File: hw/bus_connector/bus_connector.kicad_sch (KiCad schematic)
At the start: 9 parts, among them J1 DE9_Left, J2 DE9_Top, J3 DE9_Right

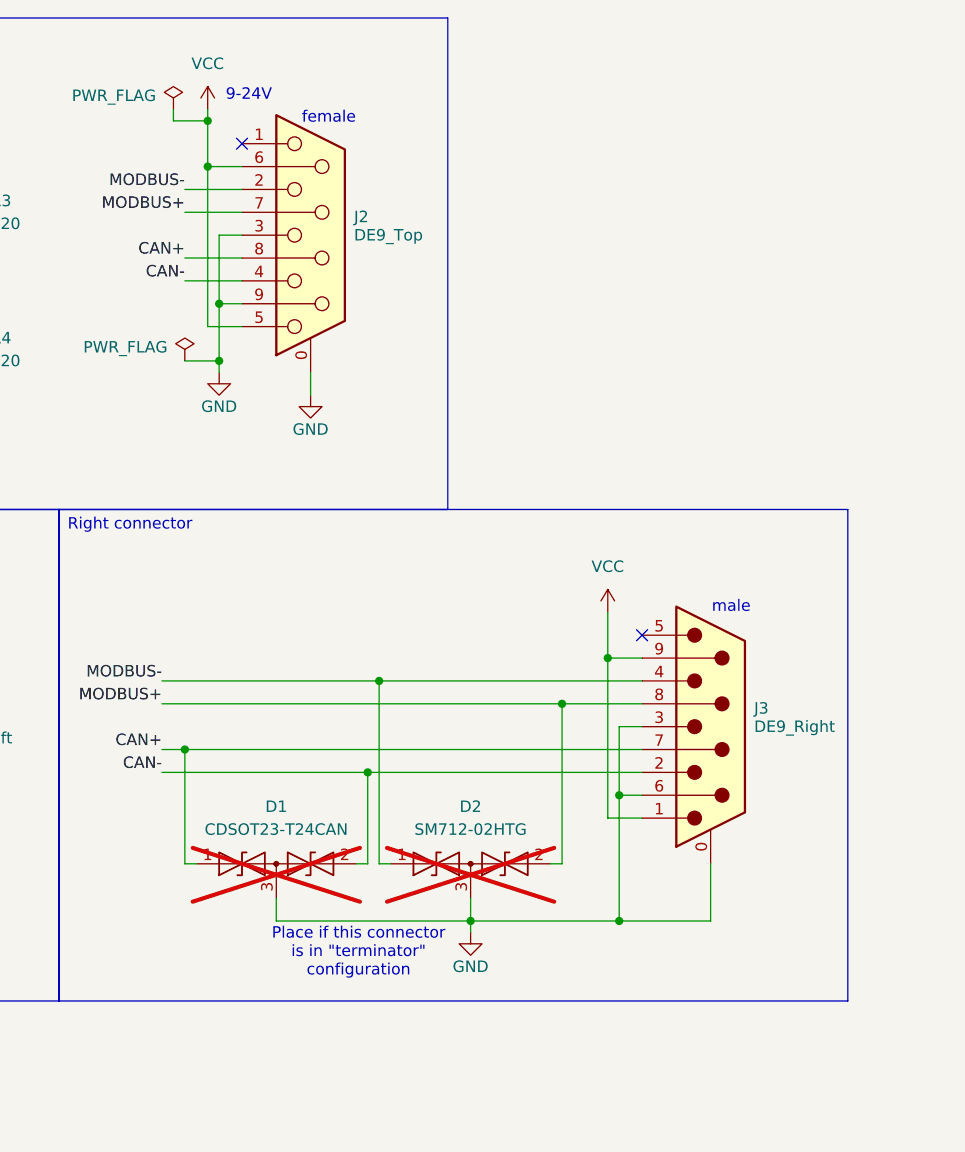
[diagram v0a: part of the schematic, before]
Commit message: Add test points
Signed-off-by: Mateusz Pająk <22417805+Tai-Min@users.noreply.github.com>
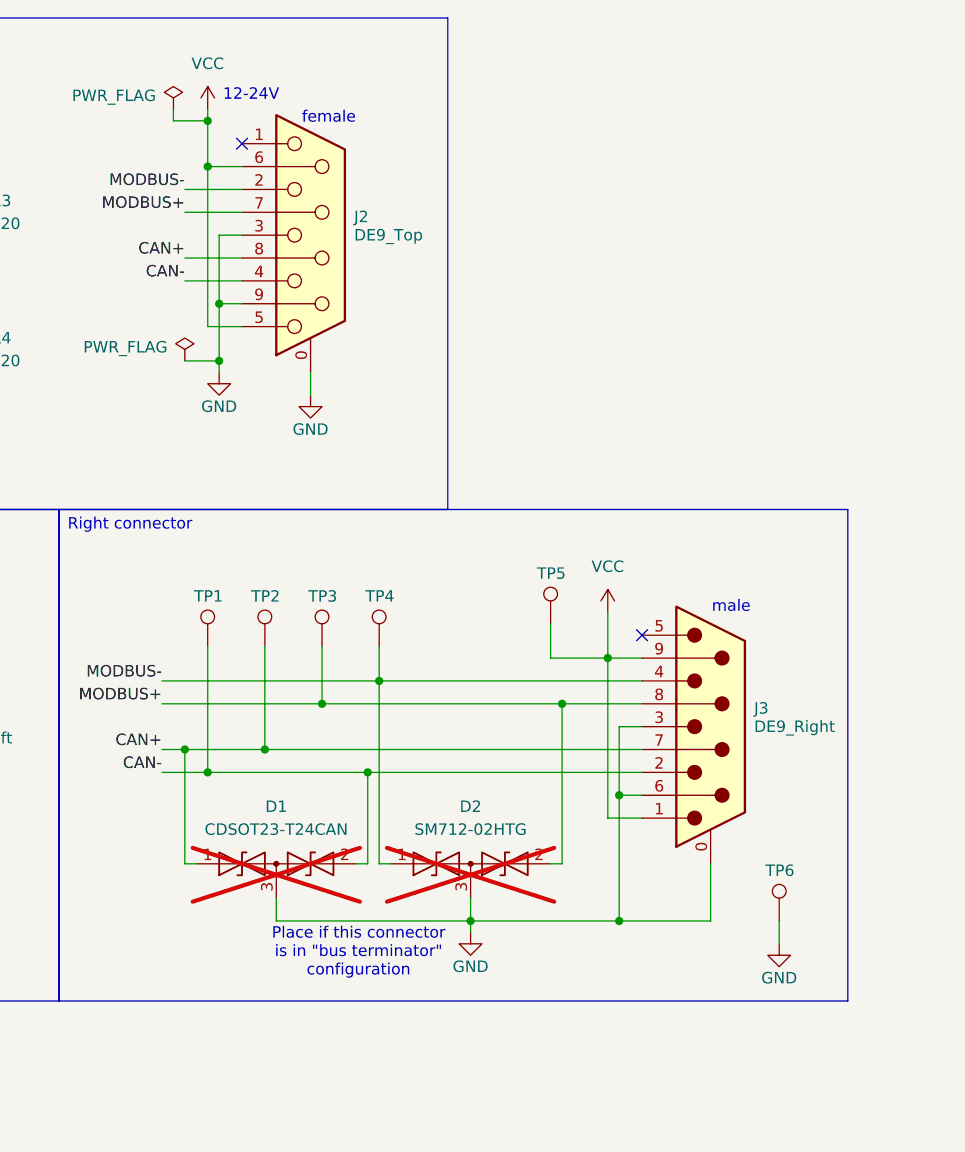
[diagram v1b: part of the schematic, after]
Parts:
- added TP1, TP2, TP3, TP4, TP5, TP6: TestPoint, TestPoint:TestPoint_Pad_D1.5mm, symbol Connector:TestPoint
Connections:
- net CAN+: now also TP2.1
- net CAN-: now also TP1.1
- net GND: now also TP6.1
- net MODBUS+: now also TP3.1
- net MODBUS-: now also TP4.1
- net VCC: now also TP5.1
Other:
- note added: "12-24V"
- note removed: "9-24V"
- note removed: "Place if this connector is in "terminator" configuration"

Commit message: Change versioning
Signed-off-by: Mateusz Pająk <22417805+Tai-Min@users.noreply.github.com>
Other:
- note added: "Place if this connector is in "bus terminator" or "bus connector" configuration"
- title: Bus Connector -> ${TITLE}
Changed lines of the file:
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@@
 	(paper "A4")
 	(title_block
-		(title "Bus Connector")
+		(title "${TITLE}")
 		(date "2025-11-24")
-		(rev "1.0")
+		(rev "${REVISION}")
 	)
 	(rectangle
@@
 		)
 	)
-	(text "Place if this connector\nis in \"bus terminator\" \nconfiguration"
+	(text "Place if this connector\nis in \"bus terminator\" or \n\"bus connector\" configuration"
 		(exclude_from_sim no)
-		(at 185.674 140.716 0)
+		(at 181.356 140.716 0)
 		(effects
 			(font

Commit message: Redo vias and VCC
Signed-off-by: Mateusz Pająk <22417805+Tai-Min@users.noreply.github.com>
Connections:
- net CAN+: now also D1.2 (A2); no longer D1.1 (A1)
- net CAN-: now also D1.1 (A1); no longer D1.2 (A2)
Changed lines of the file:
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@@
 		(lib_id "Diode:SM712_SOT23")
 		(at 176.53 130.81 0)
+		(mirror y)
 		(unit 1)
 		(exclude_from_sim no)
@@
 		(on_board yes)
 		(dnp yes)
-		(fields_autoplaced yes)
 		(property "Reference" "D1"
 			(at 176.53 124.46 0)
@@
 		)
 		(property "Datasheet" "\\datasheets\\CDSOT23-T24CAN.pdf"
-			(at 172.72 130.81 0)
+			(at 180.34 130.81 0)
 			(effects
 				(font

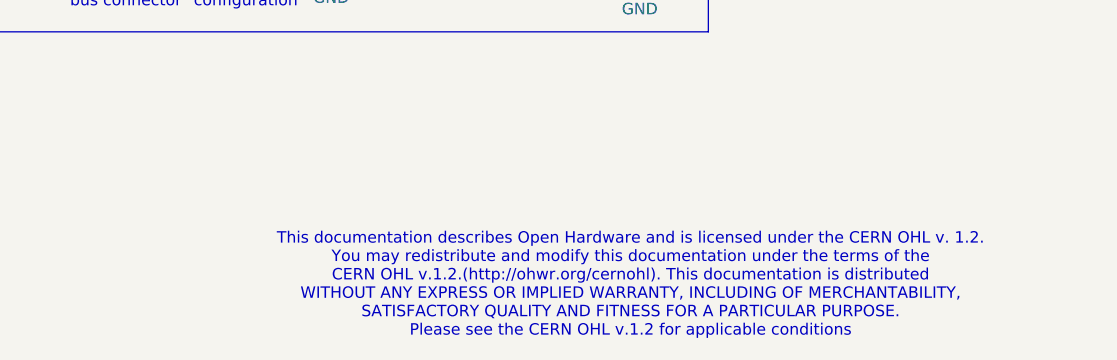
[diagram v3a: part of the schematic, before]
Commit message: Add proper drawing sheet with license
Signed-off-by: Mateusz Pająk <22417805+Tai-Min@users.noreply.github.com>
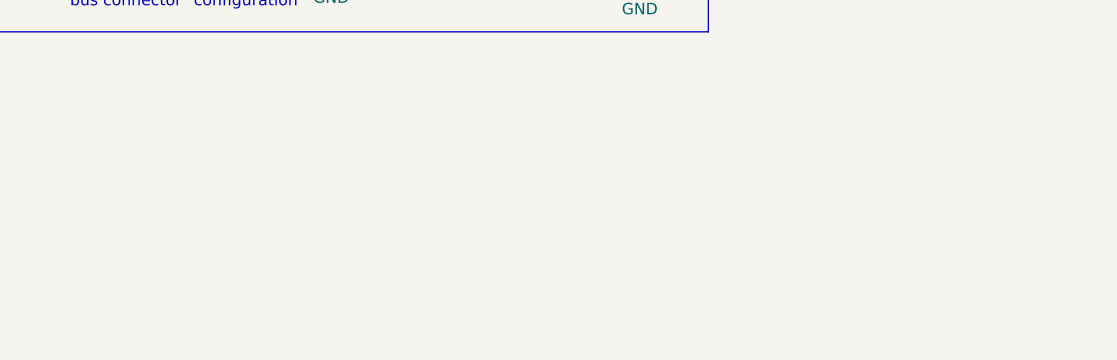
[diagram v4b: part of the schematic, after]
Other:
- note removed: "This documentation describes Open Hardware and is licensed under the CERN OHL v. 1.2. You may redistribute and modify this documentation under the terms of the CERN OHL v.1.2.(http://ohwr.org/cernohl). This documentation is distributed WITHOUT ANY EXPRESS OR IMPLIED WARRANTY, INCLUDING OF MERCHANTABILITY, SATISFACTORY QUALITY AND FITNESS FOR A PARTICULAR PURPOSE. Please see the CERN OHL v.1.2 for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"
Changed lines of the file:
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@@
-		)
-	)
-	(text "This documentation describes Open Hardware and is licensed under the CERN OHL v. 1.2.\nYou may redistribute and modify this documentation under the terms of the \nCERN OHL v.1.2.(http://ohwr.org/cernohl). This documentation is distributed \nWITHOUT ANY EXPRESS OR IMPLIED WARRANTY, INCLUDING OF MERCHANTABILITY,\nSATISFACTORY QUALITY AND FITNESS FOR A PARTICULAR PURPOSE.\nPlease see the CERN OHL v.1.2 for applicable conditions"
-		(exclude_from_sim no)
-		(at 231.394 174.244 0)
-		(effects
-			(font
-				(size 1.27 1.27)
-			)
 		)
 	)
@@
 	)
 	(embedded_fonts no)
+	(embedded_files
+		(file
+			(name "drawing_sheet.kicad_wks")
+			(type worksheet)
+			(data |KLUv/WAhCq0bANZtjiDgWjeUd7GfIpdQ3hsyJE4imh40WCrg3bHZNmcww0sw4IEAhQCDAL5lJzOj
+				pT+67/YvbT+xKmvrmW/8KFQ2Oef8xK9I+Farb213mmX+KIu3+RqV985lKu8S6eqtOr4kbVGiPXrU
+				0FVt89I+L+vxRQ2dVv1fN92t3wUAICBIqfanm+bIRNk9X4SmMtd5W/34SYZGrTXBbZzjfFP9qwIg
+				IEhPLNFpzXsqBJlvi9J55PpTNhS/0Av/dccTzaUrOLDziasXG43MLVVTuGOrGQ04il9HJPEioAVG
+				6LTOt1od2sIZjdhHehLRxxlHEEbwx28r0Vq79G/8prtGd6cqU8d59Vxc51tZlltNFAAb51H1jvM0
+				p7Ka+W79Lne3JTrOt87V0ia+237qtX6ss7lR3wKlAg6Nsqco/XufGbVV5dU7vedrd1mUqzIIhzRO
+				q66t/FLReEb8Iv6l7fpPrPLzU/zmRT29fmLrry3r1Lbi+FMaT7+82kz/dJzvtiozn57eErfgOgej
+				Qnoh+X2VsdFIaAqMl/ku4OROzIvafZ2hbfW7kCCJ7ktylavn9f1fGgeI2OAEAwGBgds6bcG5o+HQ
+				GOk9cTb90dKaF02lrP+n/ql9NMQh7Rs1ocgJXfQunAhIil7o3iRDghOXeJyNg0QNGfEmI0h6Iw6B
+				FxDiVSLih/GJxikZUMK5RDKgH0BkxhNFz+OSD7yEGNBFjY/jJ4afz0EZz0mOpkKCntM1A1rKWL+J
+				IOmsaVYpIxCP1N4BgIagATmGmBkakSCSpCDJcGBExMxVN+ZEMIr2+Ixg+w44oI2QkWfDYQBGWKkF
+				Mwg4uwAUEVRASQ6CoSO7wOH2oRcJQ92PVxKzOyKxApiF5j1bCYde/8e8NSfJCOTZBjnL5kEgk9zl
+				MlBII26C1dPzpy84m5fIib7lme/qD5PyoQz2EJoQE1jDRgTxITi8ia/sl5+zrDxPhKBBn57ycYJg
+				ZCwqHFwyZdBoqHYp0zBZO06dzgfsT4kYixZyxQyfvGf1jGnpkx8aKmozkcOWchtBzaWzZv2hQIju
+				lOqJaiUvzvCA3LzBdbUVIJOYJSx0+3ufDFvX5dIvDoxARYL0gCYirRADAnCnk8CcCCxLwcP0pwGD
+				AcdTPbjcedGBdAsSMjEiw0/8xNymVps2TR/W8jcsl1Bj2egAHQNMBQ==|
+			)
+			(checksum "F4CA3C5331BFF1A6D590C818164A77B8")
+		)
+	)
 )

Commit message: Update LCSC BOM
Signed-off-by: Mateusz Pająk <22417805+Tai-Min@users.noreply.github.com>
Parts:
- D1: LCSC https://www.lcsc.com/product-detail/C2959841.html?s_z=n_CDS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 -> (none); LCSC Link (none) -> https://www.lcsc.com/product-detail/C2959841.html?s_z=n_CDS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; LCSC Part # (none) -> C2959841
- D2: LCSC https://www.lcsc.com/product-detail/C172881.html?s_z=n_SM712 -> (none); LCSC Link (none) -> https://www.lcsc.com/product-detail/C172881.html?s_z=n_SM712; LCSC Part # (none) -> C172881
- J1, J2: LCSC https://www.lcsc.com/product-detail/C19077337.html?s_z=n_XU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 -> (none); LCSC Link (none) -> https://www.lcsc.com/product-detail/C19077337.html?s_z=n_XU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; LCSC Part # (none) -> C19077337
- J3: LCSC https://www.lcsc.com/product-detail/C19077344.html?s_z=n_ds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 -> (none); LCSC Link (none) -> https://www.lcsc.com/product-detail/C19077344.html?s_z=n_ds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; LCSC Part # (none) -> C19077344
- R1, R2, R3, R4: LCSC https://www.lcsc.com/product-detail/C114928.html -> (none); LCSC Link (none) -> https://www.lcsc.com/product-detail/C114928.html; LCSC Part # (none) -> C114928
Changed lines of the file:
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@@
 			)
 		)
-		(property "LCSC" "https://www.lcsc.com/product-detail/C114928.html"
+		(property "LCSC Link" "https://www.lcsc.com/product-detail/C114928.html"
+			(at 96.52 119.38 0)
+			(effects
+				(font
+					(size 1.27 1.27)
+				)
+				(hide yes)
+			)
+		)
+		(property "LCSC Part #" "C114928"
 			(at 96.52 119.38 0)
 			(effects
@@
 			)
 		)
+		(property "LCSC Part #" ""
+			(at 168.91 106.68 0)
+			(effects
+				(font
+					(size 1.27 1.27)
+				)
+				(hide yes)
+			)
+		)
 		(pin "1"
 		)
@@
 			)
 		)
-		(property "LCSC" "https://www.lcsc.com/product-detail/C19077344.html?s_z=n_dsub"
+		(property "LCSC Link" "https://www.lcsc.com/product-detail/C19077344.html?s_z=n_dsub"
+			(at 224.79 115.57 0)
+			(effects
+				(font
+					(size 1.27 1.27)
+				)
+				(hide yes)
+			)
+		)
+		(property "LCSC Part #" "C19077344"
 			(at 224.79 115.57 0)
 			(effects
@@
 		)
 		(property "Description" "test point"
+			(at 232.41 137.16 0)
+			(effects
+				(font
+					(size 1.27 1.27)
+				)
+				(hide yes)
+			)
+		)
+		(property "LCSC Part #" ""
 			(at 232.41 137.16 0)
 			(effects
@@
 			)
 		)
-		(property "LCSC" "https://www.lcsc.com/product-detail/C114928.html"
+		(property "LCSC Link" "https://www.lcsc.com/product-detail/C114928.html"
+			(at 142.24 58.42 0)
+			(effects
+				(font
+					(size 1.27 1.27)
+				)
+				(hide yes)
+			)
+		)
+		(property "LCSC Part #" "C114928"
 			(at 142.24 58.42 0)
 			(effects
@@
 		)
 		(property "Description" "test point"
+			(at 187.96 106.68 0)
+			(effects
+				(font
+					(size 1.27 1.27)
+				)
+				(hide yes)
+			)
+		)
+		(property "LCSC Part #" ""
 			(at 187.96 106.68 0)
 			(effects
@@
 			)
 		)
-		(property "LCSC" "https://www.lcsc.com/product-detail/C114928.html"
+		(property "LCSC Link" "https://www.lcsc.com/product-detail/C114928.html"
+			(at 142.24 73.66 0)
+			(effects
+				(font
+					(size 1.27 1.27)
+				)
+				(hide yes)
+			)
+		)
+		(property "LCSC Part #" "C114928"
 			(at 142.24 73.66 0)
 			(effects
@@
 			)
 		)
+		(property "LCSC Part #" ""
+			(at 181.61 106.68 0)
+			(effects
+				(font
+					(size 1.27 1.27)
+				)
+				(hide yes)
+			)
+		)
 		(pin "1"
 		)
@@
 			)
 		)
-		(property "LCSC" "https://www.lcsc.com/product-detail/C114928.html"
+		(property "LCSC Link" "https://www.lcsc.com/product-detail/C114928.html"
+			(at 96.52 104.14 0)
+			(effects
+				(font
+					(size 1.27 1.27)
+				)
+				(hide yes)
+			)
+		)
+		(property "LCSC Part #" "C114928"
 			(at 96.52 104.14 0)
 			(effects
@@
 		)
 		(property "Description" "test point"
+			(at 175.26 106.68 0)
+			(effects
+				(font
+					(size 1.27 1.27)
+				)
+				(hide yes)
+			)
+		)
+		(property "LCSC Part #" ""
 			(at 175.26 106.68 0)
 			(effects
@@
 			)
 		)
-		(property "LCSC" "https://www.lcsc.com/product-detail/C172881.html?s_z=n_SM712"
+		(property "LCSC Link" "https://www.lcsc.com/product-detail/C172881.html?s_z=n_SM712"
+			(at 198.12 130.81 0)
+			(effects
+				(font
+					(size 1.27 1.27)
+				)
+				(hide yes)
+			)
+		)
+		(property "LCSC Part #" "C172881"
 			(at 198.12 130.81 0)
 			(effects
@@
 			)
 		)
-		(property "LCSC" "https://www.lcsc.com/product-detail/C2959841.html?s_z=n_CDSOT23-T24CAN"
+		(property "LCSC Link" "https://www.lcsc.com/product-detail/C2959841.html?s_z=n_CDSOT23-T24CAN"
+			(at 176.53 130.81 0)
+			(effects
+				(font
+					(size 1.27 1.27)
+				)
+				(hide yes)
+			)
+		)
+		(property "LCSC Part #" "C2959841"
 			(at 176.53 130.81 0)
 			(effects
@@
 			)
 		)
-		(property "LCSC" "https://www.lcsc.com/product-detail/C19077337.html?s_z=n_XUNPU%2520D-SUB-DR-9"
+		(property "LCSC Link" "https://www.lcsc.com/product-detail/C19077337.html?s_z=n_XUNPU%2520D-SUB-DR-9"
+			(at 134.62 116.84 0)
+			(effects
+				(font
+					(size 1.27 1.27)
+				)
+				(hide yes)
+			)
+		)
+		(property "LCSC Part #" "C19077337"
 			(at 134.62 116.84 0)
 			(effects
@@
 			)
 		)
+		(property "LCSC Part #" ""
+			(at 207.01 104.14 0)
+			(effects
+				(font
+					(size 1.27 1.27)
+				)
+				(hide yes)
+			)
+		)
 		(pin "1"
 		)
@@
 			)
 		)
-		(property "LCSC" "https://www.lcsc.com/product-detail/C19077337.html?s_z=n_XUNPU%2520D-SUB-DR-9"
+		(property "LCSC Link" "https://www.lcsc.com/product-detail/C19077337.html?s_z=n_XUNPU%2520D-SUB-DR-9"
 			(at 180.34 60.96 0)
 			(effects
+				(font
+					(size 1.27 1.27)
+				)
+				(hide yes)
+			)
+		)
+		(property "LCSC Part #" "C19077337"
+			(at 180.34 60.96 0)
+			(effects

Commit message: Update LCSC BOM
Signed-off-by: Mateusz Pająk <22417805+Tai-Min@users.noreply.github.com>
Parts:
- D1: LCSC Link https://www.lcsc.com/product-detail/C2959841.html?s_z=n_CDS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 -> (none)
- D2: LCSC Link https://www.lcsc.com/product-detail/C172881.html?s_z=n_SM712 -> (none)
- J1, J2: LCSC Link https://www.lcsc.com/product-detail/C19077337.html?s_z=n_XU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 -> (none)
- J3: LCSC Link https://www.lcsc.com/product-detail/C19077344.html?s_z=n_ds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 -> (none)
- R1, R2, R3, R4: LCSC Link https://www.lcsc.com/product-detail/C114928.html -> (none)
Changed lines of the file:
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@@
-			)
-		)
-		(property "LCSC Link" "https://www.lcsc.com/product-detail/C114928.html"
-			(at 96.52 119.38 0)
-			(effects
-				(font
-					(size 1.27 1.27)
-				)
-				(hide yes)
 			)
 		)
@@
 		)
 		(property "Description" "9-pin D-SUB connector, pins (male), Mounting Hole"
-			(at 224.79 115.57 0)
-			(effects
-				(font
-					(size 1.27 1.27)
-				)
-				(hide yes)
-			)
-		)
-		(property "LCSC Link" "https://www.lcsc.com/product-detail/C19077344.html?s_z=n_dsub"
 			(at 224.79 115.57 0)
 			(effects
@@
 			)
 		)
-		(property "LCSC Link" "https://www.lcsc.com/product-detail/C114928.html"
-			(at 142.24 58.42 0)
-			(effects
-				(font
-					(size 1.27 1.27)
-				)
-				(hide yes)
-			)
-		)
 		(property "LCSC Part #" "C114928"
 			(at 142.24 58.42 0)
@@
 			)
 		)
-		(property "LCSC Link" "https://www.lcsc.com/product-detail/C114928.html"
-			(at 142.24 73.66 0)
-			(effects
-				(font
-					(size 1.27 1.27)
-				)
-				(hide yes)
-			)
-		)
 		(property "LCSC Part #" "C114928"
 			(at 142.24 73.66 0)
@@
 			)
 		)
-		(property "LCSC Link" "https://www.lcsc.com/product-detail/C114928.html"
-			(at 96.52 104.14 0)
-			(effects
-				(font
-					(size 1.27 1.27)
-				)
-				(hide yes)
-			)
-		)
 		(property "LCSC Part #" "C114928"
 			(at 96.52 104.14 0)
@@
 			)
 		)
-		(property "LCSC Link" "https://www.lcsc.com/product-detail/C172881.html?s_z=n_SM712"
-			(at 198.12 130.81 0)
-			(effects
-				(font
-					(size 1.27 1.27)
-				)
-				(hide yes)
-			)
-		)
 		(property "LCSC Part #" "C172881"
 			(at 198.12 130.81 0)
@@
 			)
 		)
-		(property "LCSC Link" "https://www.lcsc.com/product-detail/C2959841.html?s_z=n_CDSOT23-T24CAN"
-			(at 176.53 130.81 0)
-			(effects
-				(font
-					(size 1.27 1.27)
-				)
-				(hide yes)
-			)
-		)
 		(property "LCSC Part #" "C2959841"
 			(at 176.53 130.81 0)
@@
 			)
 		)
-		(property "LCSC Link" "https://www.lcsc.com/product-detail/C19077337.html?s_z=n_XUNPU%2520D-SUB-DR-9"
-			(at 134.62 116.84 0)
-			(effects
-				(font
-					(size 1.27 1.27)
-				)
-				(hide yes)
-			)
-		)
 		(property "LCSC Part #" "C19077337"
 			(at 134.62 116.84 0)
@@
 			(effects
 				(font
-					(size 1.27 1.27)
-				)
-				(hide yes)
-			)
-		)
-		(property "LCSC Link" "https://www.lcsc.com/product-detail/C19077337.html?s_z=n_XUNPU%2520D-SUB-DR-9"
-			(at 180.34 60.96 0)
-			(effects
-				(font
